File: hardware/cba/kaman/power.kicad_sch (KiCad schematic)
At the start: 0 parts

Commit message: hw(schematic): add the power section
Three power sources USB, DC Jack and simple 2.54mm connector with a
schottkey diode on USB and simple ones to block reverse current into a
AZ1117 and outputs 3.3v
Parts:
- added C14, C15: 10uF, Capacitor_SMD:C_0805_2012Metric_Pad1.18x1.45mm_HandSolder, symbol Device:C
- added D7, D9: 1N5819WT, Diode_SMD:D_SOD-523, symbol Diode:1N5819WS
- added D8: SD05C-01F, Diode_SMD:D_SOD-323, symbol Diode:SD05C-01F
- added J3: Barrel_Jack_MountingPin, Connector_BarrelJack:BarrelJack_GCT_DCJ200-10-A_Horizontal, symbol Connector:Barrel_Jack_MountingPin
- added J5: Conn_01x02_Socket, Connector_PinHeader_2.54mm:PinHeader_1x02_P2.54mm_Vertical, symbol Connector:Conn_01x02_Socket
- added U5: AZ1117-3.3, Package_TO_SOT_SMD:SOT-89-3_Handsoldering, symbol Regulator_Linear:AZ1117-3.3
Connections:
- new net: D7.2 (A), D9.2 (A), J5.2 (Pin_2)
- new net +3.3V: C15.1, D8.2 (A2), U5.2 (VO)
- new net GND: C14.2, C15.2, D8.1 (A1), J3.2, J3.MP (MountPin), J5.1 (Pin_1), U5.1 (GND)
- new net VDD: C14.1, D7.1 (K), D9.1 (K), J3.1, U5.3 (VI)

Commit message: hw(schematic): Change reverse current diodes
The previous schottky 1N5819WT is rated for 350mA which needs two for
maximum of 700mA and is repalced with DFLS160-7 which is rated for 1A
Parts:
- removed D7, D9: 1N5819WT, Diode_SMD:D_SOD-523, symbol Diode:1N5819WS
- added D6: DFLS160-7, Diode_SMD:D_PowerDI-123, symbol Device:D_Schottky
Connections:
- net VDD: now also D6.1 (K)
- net at J5.2 (Pin_2): now also D6.2 (A)
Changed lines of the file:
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@@
-	)
-	(junction
-		(at 27.94 17.78)
-		(diameter 0)
-		(color 0 0 0 0)
 	)
 	(junction
@@
 		(color 0 0 0 0)
 	)
-	(junction
-		(at 36.83 21.59)
-		(diameter 0)
-		(color 0 0 0 0)
-	)
-	(wire
-		(pts
-			(xy 35.56 21.59) (xy 36.83 21.59)
-		)
-		(stroke
-			(width 0)
-			(type default)
-		)
-	)
-	(wire
-		(pts
-			(xy 36.83 21.59) (xy 36.83 26.67)
-		)
-		(stroke
-			(width 0)
-			(type default)
-		)
-	)
-	(wire
-		(pts
-			(xy 27.94 17.78) (xy 27.94 21.59)
+	(wire
+		(pts
+			(xy 36.83 17.78) (xy 36.83 26.67)
 		)
 		(stroke
@@
 		(pts
 			(xy 64.77 26.67) (xy 67.31 26.67)
-		)
-		(stroke
-			(width 0)
-			(type default)
-		)
-	)
-	(wire
-		(pts
-			(xy 36.83 17.78) (xy 36.83 21.59)
 		)
 		(stroke
@@
 	)
 	(symbol
+		(lib_id "Device:D_Schottky")
+		(at 31.75 17.78 0)
+		(mirror y)
+		(unit 1)
+		(body_style 1)
+		(exclude_from_sim no)
+		(in_bom yes)
+		(on_board yes)
+		(in_pos_files yes)
+		(dnp no)
+		(property "Reference" "D6"
+			(at 31.75 15.24 0)
+			(show_name no)
+			(do_not_autoplace no)
+			(effects
+				(font
+					(size 1.27 1.27)
+				)
+			)
+		)
+		(property "Value" "DFLS160-7"
+			(at 32.0675 13.97 0)
+			(hide yes)
+			(show_name no)
+			(do_not_autoplace no)
+			(effects
+				(font
+					(size 1.27 1.27)
+				)
+			)
+		)
+		(property "Footprint" "Diode_SMD:D_PowerDI-123"
+			(at 31.75 17.78 0)
+			(hide yes)
+			(show_name no)
+			(do_not_autoplace no)
+			(effects
+				(font
+					(size 1.27 1.27)
+				)
+			)
+		)
+		(property "Datasheet" ""
+			(at 31.75 17.78 0)
+			(hide yes)
+			(show_name no)
+			(do_not_autoplace no)
+			(effects
+				(font
+					(size 1.27 1.27)
+				)
+			)
+		)
+		(property "Description" "Schottky diode"
+			(at 31.75 17.78 0)
+			(hide yes)
+			(show_name no)
+			(do_not_autoplace no)
+			(effects
+				(font
+					(size 1.27 1.27)
+				)
+			)
+		)
+		(pin "2"
+		)
+		(pin "1"
+		)
+		(instances
+			(project "Template"
+				(path "/b7abe575-2b7a-4e47-9046-9769d7102f9d/c3e404eb-2e1f-4ab9-8da3-bc1a9ff0af28/06162593-d836-449e-9de8-3662ea444cd9"
+					(reference "D6")
+					(unit 1)
+				)
+			)
+		)
+	)
+	(symbol
 		(lib_id "power:GND")
 		(at 41.91 34.29 0)
@@
 					(unit 1)
 				)
-			)
-		)
-	)
-	(symbol
-		(lib_id "Diode:1N5819WS")
-		(at 31.75 21.59 180)
-		(unit 1)
-		(body_style 1)
-		(exclude_from_sim no)
-		(in_bom yes)
-		(on_board yes)
-		(in_pos_files yes)
-		(dnp no)
-		(property "Reference" "D7"
-			(at 34.798 20.32 0)
-			(show_name no)
-			(do_not_autoplace no)
-			(effects
-				(font
-					(size 1.27 1.27)
-				)
-			)
-		)
-		(property "Value" "1N5819WT"
-			(at 32.0675 17.78 0)
-			(hide yes)
-			(show_name no)
-			(do_not_autoplace no)
-			(effects
-				(font
-					(size 1.27 1.27)
-				)
-			)
-		)
-		(property "Footprint" "Diode_SMD:D_SOD-523"
-			(at 31.75 17.145 0)
-			(hide yes)
-			(show_name no)
-			(do_not_autoplace no)
-			(effects
-				(font
-					(size 1.27 1.27)
-				)
-			)
-		)
-		(property "Datasheet" "https://datasheet.lcsc.com/lcsc/2204281430_Guangdong-Hottech-1N5819WS_C191023.pdf"
-			(at 31.75 21.59 0)
-			(hide yes)
-			(show_name no)
-			(do_not_autoplace no)
-			(effects
-				(font
-					(size 1.27 1.27)
-				)
-			)
-		)
-		(property "Description" "40V 600mV@1A 1A SOD-323 Schottky Barrier Diodes, SOD-323"
-			(at 31.75 21.59 0)
-			(hide yes)
-			(show_name no)
-			(do_not_autoplace no)
-			(effects
-				(font
-					(size 1.27 1.27)
-				)
-			)
-		)
-		(pin "1"
-		)
-		(pin "2"
-		)
-		(instances
-			(project "Template"
-				(path "/b7abe575-2b7a-4e47-9046-9769d7102f9d/c3e404eb-2e1f-4ab9-8da3-bc1a9ff0af28/06162593-d836-449e-9de8-3662ea444cd9"
-					(reference "D7")
-					(unit 1)
-				)
-			)
-		)
-	)
-	(symbol
-		(lib_id "Diode:1N5819WS")
-		(at 31.75 17.78 180)
-		(unit 1)
-		(body_style 1)
-		(exclude_from_sim no)
-		(in_bom yes)
-		(on_board yes)
-		(in_pos_files yes)
-		(dnp no)
-		(property "Reference" "D9"
-			(at 34.798 16.51 0)
-			(show_name no)
-			(do_not_autoplace no)
-			(effects
-				(font
-					(size 1.27 1.27)
-				)
-			)
-		)
-		(property "Value" "1N5819WT"
-			(at 32.0675 13.97 0)
-			(hide yes)
-			(show_name no)
-			(do_not_autoplace no)
-			(effects
-				(font
-					(size 1.27 1.27)
-				)
-			)
-		)
-		(property "Footprint" "Diode_SMD:D_SOD-523"
-			(at 31.75 13.335 0)
-			(hide yes)
-			(show_name no)
-			(do_not_autoplace no)
-			(effects
-				(font
-					(size 1.27 1.27)
-				)
-			)
-		)
-		(property "Datasheet" "https://datasheet.lcsc.com/lcsc/2204281430_Guangdong-Hottech-1N5819WS_C191023.pdf"
-			(at 31.75 17.78 0)
-			(hide yes)
-			(show_name no)
-			(do_not_autoplace no)
-			(effects
-				(font
-					(size 1.27 1.27)
-				)
-			)
-		)
-		(property "Description" "40V 600mV@1A 1A SOD-323 Schottky Barrier Diodes, SOD-323"
-			(at 31.75 17.78 0)
-			(hide yes)
-			(show_name no)
-			(do_not_autoplace no)
-			(effects
-				(font
-					(size 1.27 1.27)
-				)
-			)
-		)
-		(pin "1"
-		)
-		(pin "2"
-		)
-		(instances
-			(project "Template"
-				(path "/b7abe575-2b7a-4e47-9046-9769d7102f9d/c3e404eb-2e1f-4ab9-8da3-bc1a9ff0af28/06162593-d836-449e-9de8-3662ea444cd9"
-					(reference "D9")
-					(unit 1)
-				)

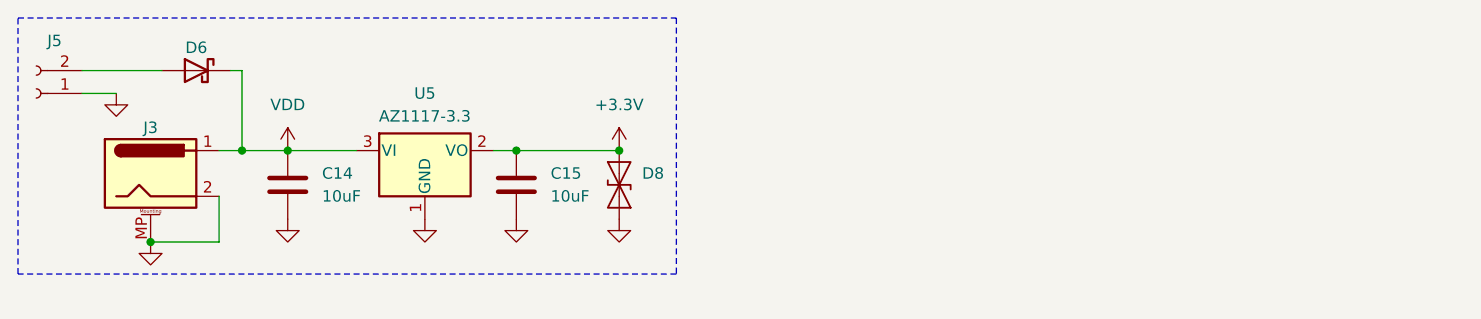
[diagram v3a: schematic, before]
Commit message: hw(schematic): add a power switch for 3.3v
To turn off the board with the input power still connected a dip switch
with a power switch has been added and it will take care of currnet
limiting to 1A and reverse currents
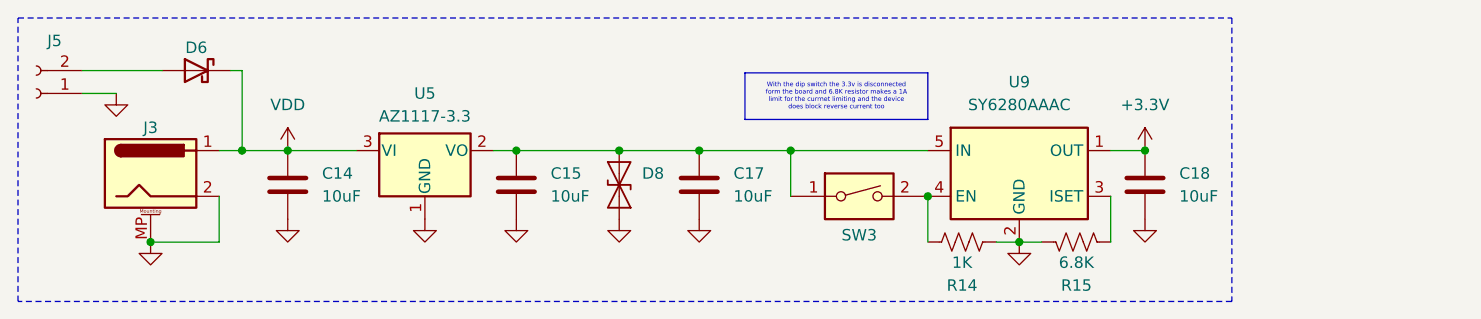
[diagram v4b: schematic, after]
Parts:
- added C17, C18: 10uF, Capacitor_SMD:C_0805_2012Metric_Pad1.18x1.45mm_HandSolder, symbol Device:C
- added R14: 1K, Resistor_SMD:R_0603_1608Metric_Pad0.98x0.95mm_HandSolder, symbol Device:R_US
- added R15: 6.8K, Resistor_SMD:R_0603_1608Metric_Pad0.98x0.95mm_HandSolder, symbol Device:R_US
- added SW3: SW_DIP_x01, Button_Switch_SMD:SW_DIP_SPSTx01_Slide_6.7x4.1mm_W8.61mm_P2.54mm_LowProfile, symbol Switch:SW_DIP_x01
- added U9: SY6280AAAC, Package_TO_SOT_SMD:SOT-23-5, symbol SY6280AAAC:SY6280AAAC
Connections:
- net +3.3V: now also C18.1, U9.1 (OUT); no longer C15.1, D8.2 (A2), U5.2 (VO)
- net GND: now also C17.2, C18.2, R14.2, R15.2, U9.2 (GND)
- new net: R15.1, U9.3 (ISET)
- new net: C15.1, C17.1, D8.2 (A2), SW3.1, U5.2 (VO), U9.5 (IN)
- new net: R14.1, SW3.2, U9.4 (EN)

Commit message: hw(schematic): add an led indicator for 3.3v
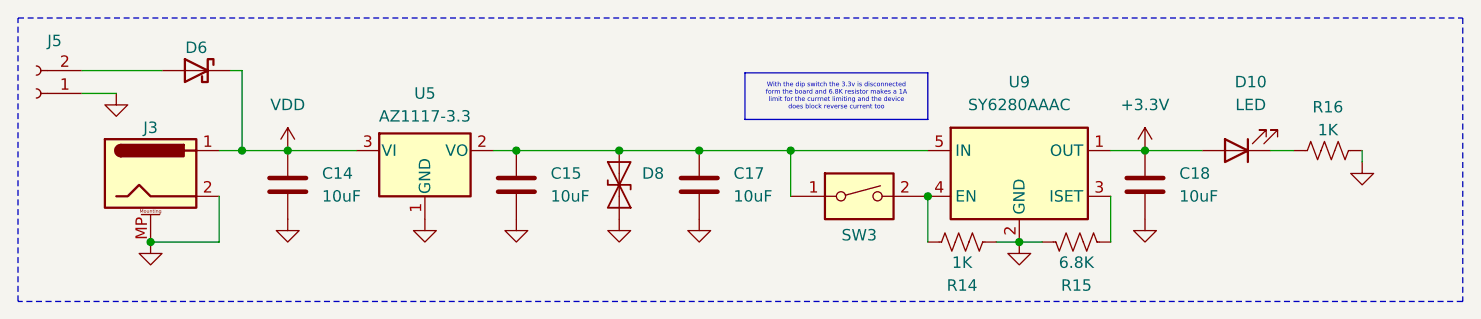
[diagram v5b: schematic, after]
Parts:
- added D10: LED, LED_SMD:LED_0603_1608Metric_Pad1.05x0.95mm_HandSolder, symbol Device:LED
- added R16: 1K, Resistor_SMD:R_0603_1608Metric_Pad0.98x0.95mm_HandSolder, symbol Device:R_US
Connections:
- net +3.3V: now also D10.2 (A)
- net GND: now also R16.1
- new net: D10.1 (K), R16.2
